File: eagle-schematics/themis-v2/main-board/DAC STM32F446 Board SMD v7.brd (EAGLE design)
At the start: 101.1 x 99.1 mm, 254 parts, among them Q1 16MHz

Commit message: Final PCB version sent to eurocircuits.com
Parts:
- removed C47, C48: 100n, rcl:C1206
- added 3V3: (no value), Passives:0805-LED
- added ANAIN: (no value), stm32_pi_board:MA02-1
- added C74, C75, C76, C77, C78, C79, C80, C81, C82, C83, C84, C85, C86, C87, C88: 1u, rcl:C1206
- added EXT: (no value), con-lstb:MA04-1
- added HOLE1, HOLE2, HOLE3, HOLE4: HOLES_MOUNT-PAD-ROUND-0.096-NS, 52101-101-REV-A:HOLES_096-PAD-NS
- added R95: 330, MyComponents:R0805
- moved +15V 13.3 mm to (97.3, 83.6)
- moved -15V 13.3 mm to (93.0, 83.6)
- moved 5V 13.3 mm to (88.6, 83.6)
- moved R92 8.01 mm to (88.5, 86.5)
- moved R93 8.01 mm to (92.8, 86.5)
- moved R94 8.01 mm to (97.2, 86.5)
- moved JACK 4.58 mm to (96.3, 12.4)
- moved C73 3.30 mm to (69.1, 15.2), flipped to the bottom, turned to 180 degrees
- moved STLINK 3.06 mm to (60.1, 37.0)
- moved C62 2.67 mm to (64.4, 66.6), flipped to the bottom, turned to 0 degrees
- moved MIXOUT 2.54 mm to (87.1, 72.9)
- moved SW2 1.92 mm to (68.8, 26.0)
- moved SW1 1.91 mm to (58.3, 26.0)
- moved L1 1.78 mm to (60.9, 60.6)
- moved R87 1.78 mm to (63.4, 60.6)
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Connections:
- new net EXT1: EXT.1, F446.50
- new net EXT2: EXT.2, F446.51
- new net EXT3: EXT.3, F446.52
- new net EXT4: EXT.4, F446.53
- new net N$57: 3V3.A, R95.2
- new net N$58: ANAIN.2, F446.16
- new net N$59: ANAIN.1, F446.17
- net +15V: now also C74.2, C77.2, C78.2, C79.2, C80.2, C81.2, C82.2, C83.2; no longer C47.2
- net -15V: now also C75.2, C84.2, C85.2, C86.2, C87.2, C88.2; no longer C48.1
- net 3V3: now also R95.1
- net 5V: now also C76.2
- net GND: now also 3V3.C, C74.1, C75.1, C76.1, C77.1, C78.1, C79.1, C80.1, C81.1, C82.1, C83.1, C84.1, C85.1, C86.1, C87.1, C88.1; no longer C47.1, C48.2
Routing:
- net GND: track 988.2 -> 1023.5 mm, vias 23 -> 25
- net N$58: track 0.00 -> 23.4 mm, vias 0 -> 1
- net N$59: track 0.00 -> 21.4 mm, vias 0 -> 2
- net EXT4: track 0.00 -> 17.8 mm
- net EXT2: track 0.00 -> 17.1 mm
- net EXT3: track 0.00 -> 17.0 mm
- net +15V: track 456.9 -> 441.0 mm
- net EXT1: track 0.00 -> 15.1 mm
- net 3V3: track 151.0 -> 162.7 mm, vias 0 -> 2
- net 5V: track 186.0 -> 197.5 mm, vias 7 -> 5
- net -15V: track 363.0 -> 367.6 mm
- net NRST: track 55.8 -> 51.3 mm
- net N$57: track 0.00 -> 3.08 mm
- net SWDIO: track 8.48 -> 5.81 mm
- net SW2: track 28.2 -> 30.8 mm, vias 2 -> 1
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- added copper zone on layer 1, net GND
- added copper zone on layer 16, net GND
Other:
- board size 101.1 x 99.1 mm -> 101.3 x 99.1 mm
- board text added: "SYD.X.REY INSTR. 2020"

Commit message: Bug fix
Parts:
- C35: value 1p -> 100p
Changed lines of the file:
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@@
 <attribute name="VALUE" x="45.974" y="78.232" size="0.3048" layer="27" ratio="10" rot="R270"/>
 </element>
-<element name="C35" library="rcl" library_urn="urn:adsk.eagle:library:334" package="C0805" package3d_urn="urn:adsk.eagle:package:23617/2" value="1p" x="80.518" y="83.312" smashed="yes">
+<element name="C35" library="rcl" library_urn="urn:adsk.eagle:library:334" package="C0805" package3d_urn="urn:adsk.eagle:package:23617/2" value="100p" x="80.518" y="83.312" smashed="yes">
 <attribute name="C3" value="0.47 micro" x="80.518" y="83.312" size="1.778" layer="27" display="off"/>
 <attribute name="NAME" x="79.248" y="81.28" size="1.016" layer="25" ratio="10"/>

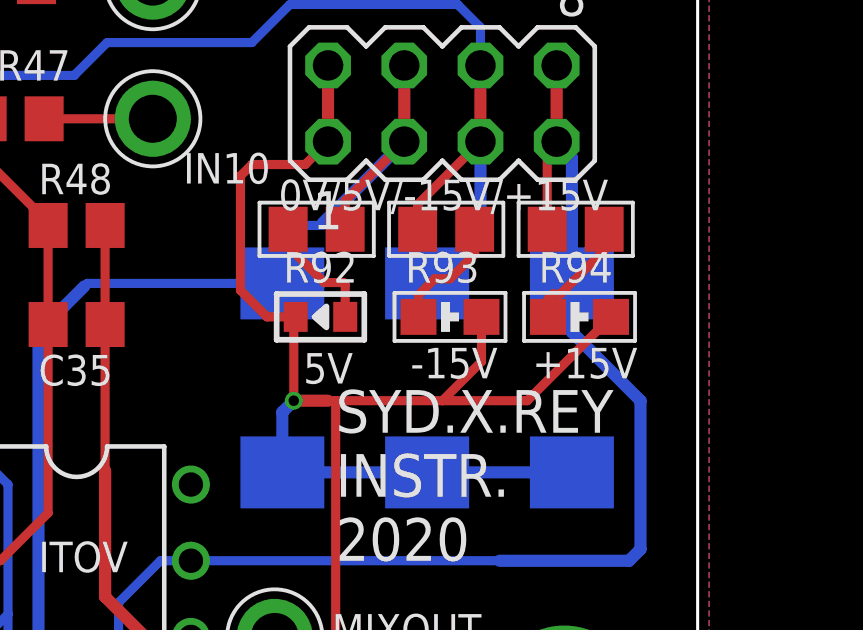
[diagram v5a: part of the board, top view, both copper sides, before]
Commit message: fixed pol cap and LED orientation errors
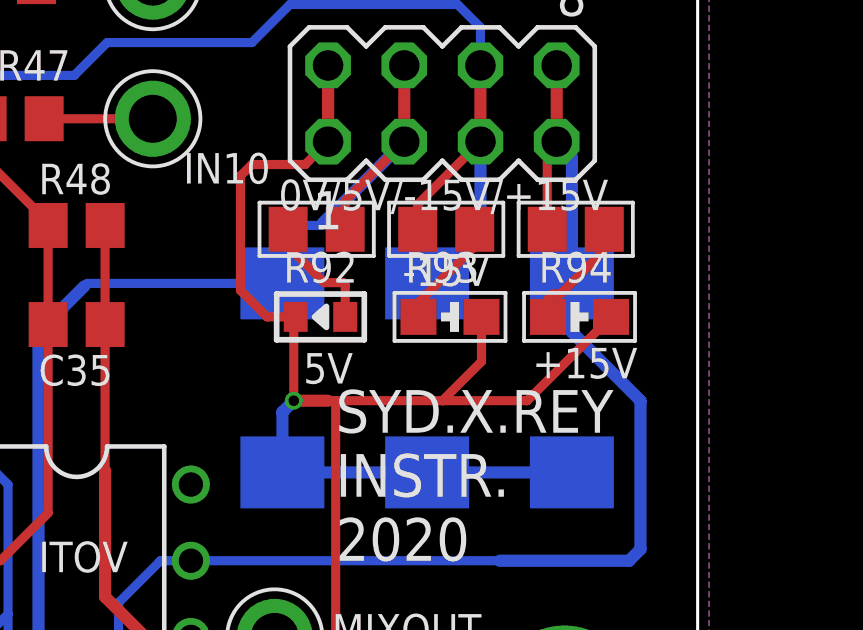
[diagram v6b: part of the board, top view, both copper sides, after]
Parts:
- R89, R91: value 330 -> 180
- R90, R95: value 330 -> 1k
- R92: value 330 -> 470
- R93, R94: value 330 -> 10k
- turned -15V to 180 degrees
- turned C54 to 90 degrees
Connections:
- net -15V: now also C54.-; no longer C54.+
- net GND: now also -15V.A, C54.+; no longer -15V.C, C54.-
- net N$54: now also -15V.C; no longer -15V.A

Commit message: Updated net names
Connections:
- net N$19 renamed BH2221_AO3
- net N$21 renamed BH2221_AO4
- net N$25 renamed BH2221_AO6
- net N$26 renamed BH2221_AO7
- net N$27 renamed BH2221_AO8
- net N$28 renamed BH2221_AO9
- net N$29 renamed BH2221_AO10
- net N$30 renamed BH2221_AO2
- net N$31 renamed BH2221_AO1
- net N$32 renamed BH2221_AO12
- net N$33 renamed BH2221_AO11
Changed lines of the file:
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@@
 <wire x1="76.2" y1="7.874" x2="77.912" y2="6.162" width="0.3048" layer="1"/>
 </signal>
-<signal name="N$26">
+<signal name="BH2221_AO7">
 <contactref element="A010/9/8/7/3/4/5/6" pad="4"/>
 <contactref element="BH2221" pad="6"/>
@@
 <wire x1="48.69050625" y1="22.52850625" x2="46.736" y2="20.574" width="0.254" layer="1"/>
 </signal>
-<signal name="N$27">
+<signal name="BH2221_AO8">
 <contactref element="A010/9/8/7/3/4/5/6" pad="3"/>
 <contactref element="BH2221" pad="7"/>
@@
 <wire x1="46.20650625" y1="20.29850625" x2="44.196" y2="18.288" width="0.254" layer="1"/>
 </signal>
-<signal name="N$28">
+<signal name="BH2221_AO9">
 <contactref element="A010/9/8/7/3/4/5/6" pad="2"/>
 <contactref element="BH2221" pad="8"/>
@@
 <wire x1="45.500496875" y1="20.862496875" x2="41.656" y2="17.018" width="0.254" layer="1"/>
 </signal>
-<signal name="N$29">
+<signal name="BH2221_AO10">
 <contactref element="A010/9/8/7/3/4/5/6" pad="1"/>
 <contactref element="BH2221" pad="9"/>
@@
 <wire x1="39.116" y1="17.018" x2="39.116" y2="16.764" width="0.254" layer="1"/>
 </signal>
-<signal name="N$30">
+<signal name="BH2221_AO2">
 <contactref element="BH2221" pad="19"/>
 <contactref element="A02/1/12/11" pad="1"/>
@@
 <wire x1="37.338" y1="20.828" x2="34.544" y2="20.828" width="0.254" layer="1"/>
 </signal>
-<signal name="N$31">
+<signal name="BH2221_AO1">
 <contactref element="BH2221" pad="18"/>
 <contactref element="A02/1/12/11" pad="2"/>
@@
 <wire x1="36.83" y1="23.368" x2="34.544" y2="23.368" width="0.254" layer="1"/>
 </signal>
-<signal name="N$32">
+<signal name="BH2221_AO12">
 <contactref element="BH2221" pad="13"/>
 <contactref element="A02/1/12/11" pad="3"/>
@@
 <wire x1="37.338" y1="25.908" x2="34.544" y2="25.908" width="0.254" layer="1"/>
 </signal>
-<signal name="N$33">
+<signal name="BH2221_AO11">
 <contactref element="A02/1/12/11" pad="4"/>
 <contactref element="BH2221" pad="12"/>
@@
 <wire x1="95.824" y1="64.262" x2="92.964" y2="64.262" width="0.3048" layer="1"/>
 </signal>
-<signal name="N$19">
+<signal name="BH2221_AO3">
 <contactref element="A010/9/8/7/3/4/5/6" pad="5"/>
 <contactref element="BH2221" pad="2"/>
@@
 <wire x1="49.1156" y1="17.1784" x2="49.276" y2="17.018" width="0.254" layer="1"/>
 </signal>
-<signal name="N$21">
+<signal name="BH2221_AO4">
 <contactref element="A010/9/8/7/3/4/5/6" pad="6"/>
 <contactref element="BH2221" pad="3"/>
@@
 <wire x1="54.356" y1="20.2921875" x2="54.356" y2="16.764" width="0.254" layer="1"/>
 </signal>
-<signal name="N$25">
+<signal name="BH2221_AO6">
 <contactref element="BH2221" pad="5"/>
 <contactref element="A010/9/8/7/3/4/5/6" pad="8"/>
